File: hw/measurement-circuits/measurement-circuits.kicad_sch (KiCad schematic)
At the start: 22 parts, among them J1 Conn_01x01_Pin, J2 Conn_01x01_Pin, J3 Conn_01x01_Pin, J4 Conn_01x01_Pin, J5 Klemme 1, U1 PC817

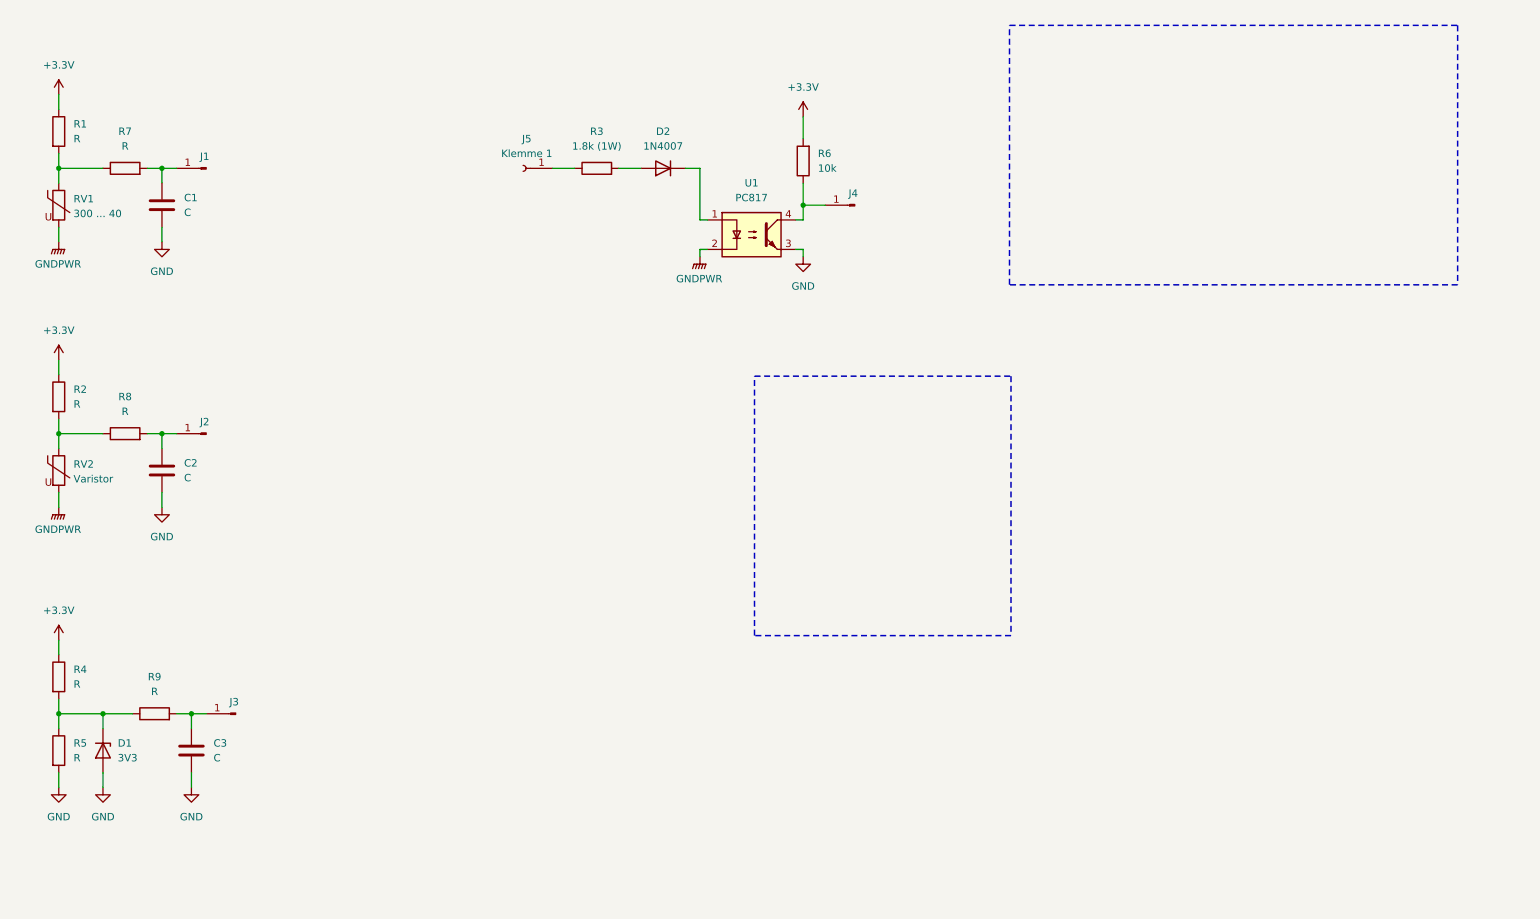
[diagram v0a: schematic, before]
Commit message: [hw/measurement-circuits] added formulas to calculate physical values
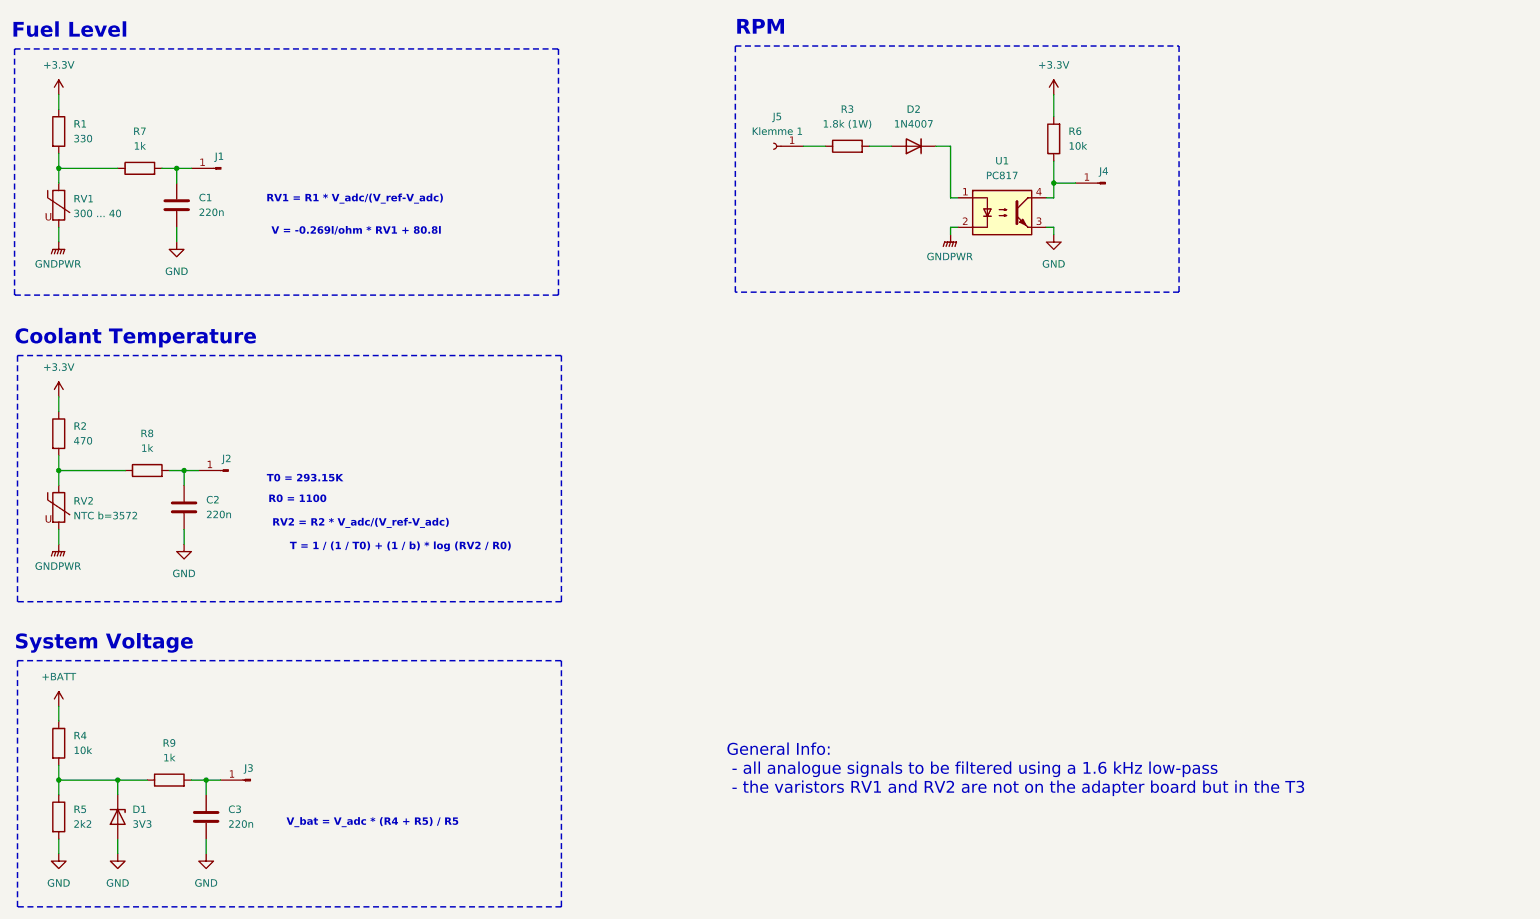
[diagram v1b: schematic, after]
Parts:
- C1, C2, C3: value C -> 220n
- R1: value R -> 330
- R2: value R -> 470
- R4: value R -> 10k
- R5: value R -> 2k2
- R7, R8, R9: value R -> 1k
- RV2: value Varistor -> NTC b=3572
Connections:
- net +3.3V: no longer R4.1
- new net +BATT: R4.1
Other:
- note added: "Coolant Temperature"
- note added: "Fuel Level"
- note added: "General Info: - all analogue signals to be filtered using a 1.6 kHz low-pass - the varistors RV1 and RV2 are not on the adapter board but in the T3"
- note added: "R0 = 1100"
- note added: "RPM"
- note added: "RV1 = R1 * V_adc/(V_ref-V_adc)"
- note added: "RV2 = R2 * V_adc/(V_ref-V_adc)"
- note added: "System Voltage"
- note added: "T = 1 / (1 / T0) + (1 / b) * log (RV2 / R0)"
- note added: "T0 = 293.15K"
- note added: "V = -0.269l/ohm * RV1 + 80.8l"
- note added: "V_bat = V_adc * (R4 + R5) / R5"
- moved on the sheet: C1, C2, C3, D1, D2, J1, J2, J3, J4, J5, R2, R3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

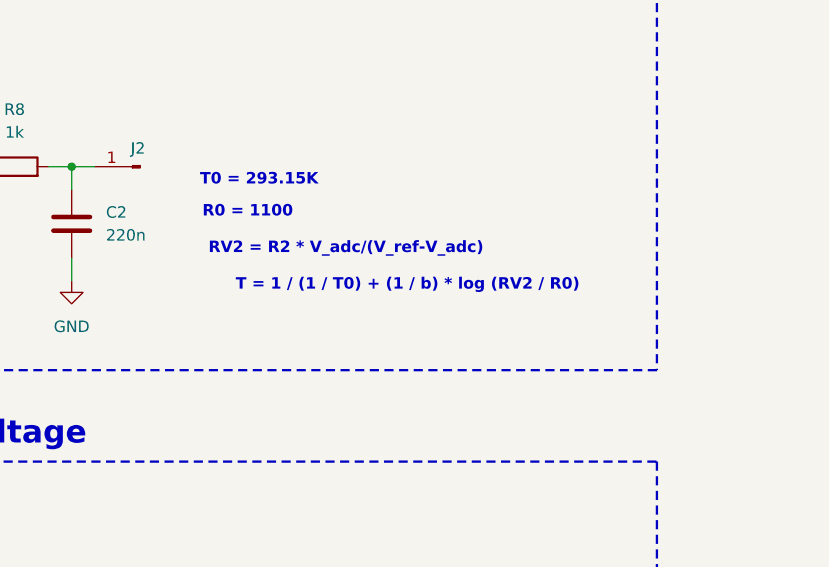
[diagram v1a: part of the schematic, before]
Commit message: [hw/measurement-circuits] fix: formula for coolant temperature
Signed-off-by: Timon Burkard <burkard.timon@gmail.com>
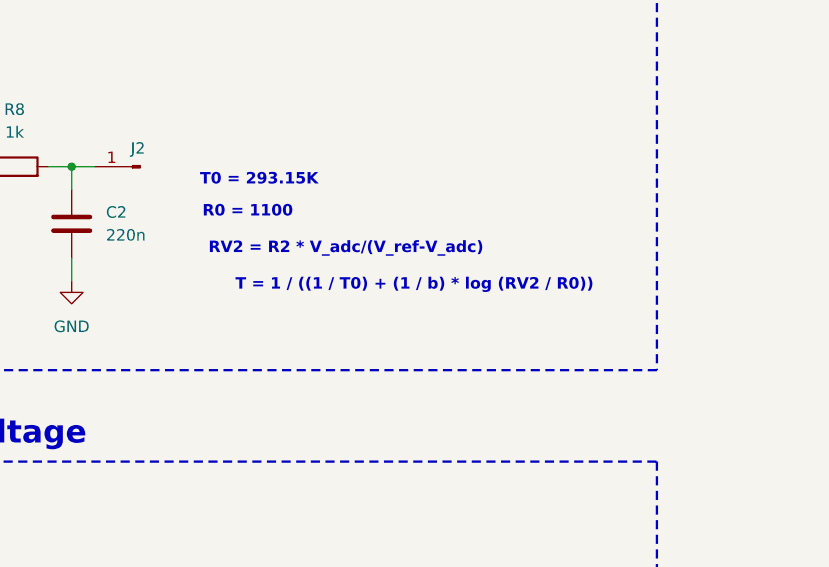
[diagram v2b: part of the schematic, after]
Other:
- note added: "T = 1 / ((1 / T0) + (1 / b) * log (RV2 / R0))"
- note removed: "T = 1 / (1 / T0) + (1 / b) * log (RV2 / R0)"
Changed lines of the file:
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@@
 		)
 	)
-	(text "T = 1 / (1 / T0) + (1 / b) * log (RV2 / R0)"
+	(text "T = 1 / ((1 / T0) + (1 / b) * log (RV2 / R0))"
 		(exclude_from_sim no)
-		(at 105.918 117.348 0)
+		(at 106.68 117.348 0)
 		(effects
 			(font
